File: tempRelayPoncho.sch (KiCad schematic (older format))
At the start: 2 parts

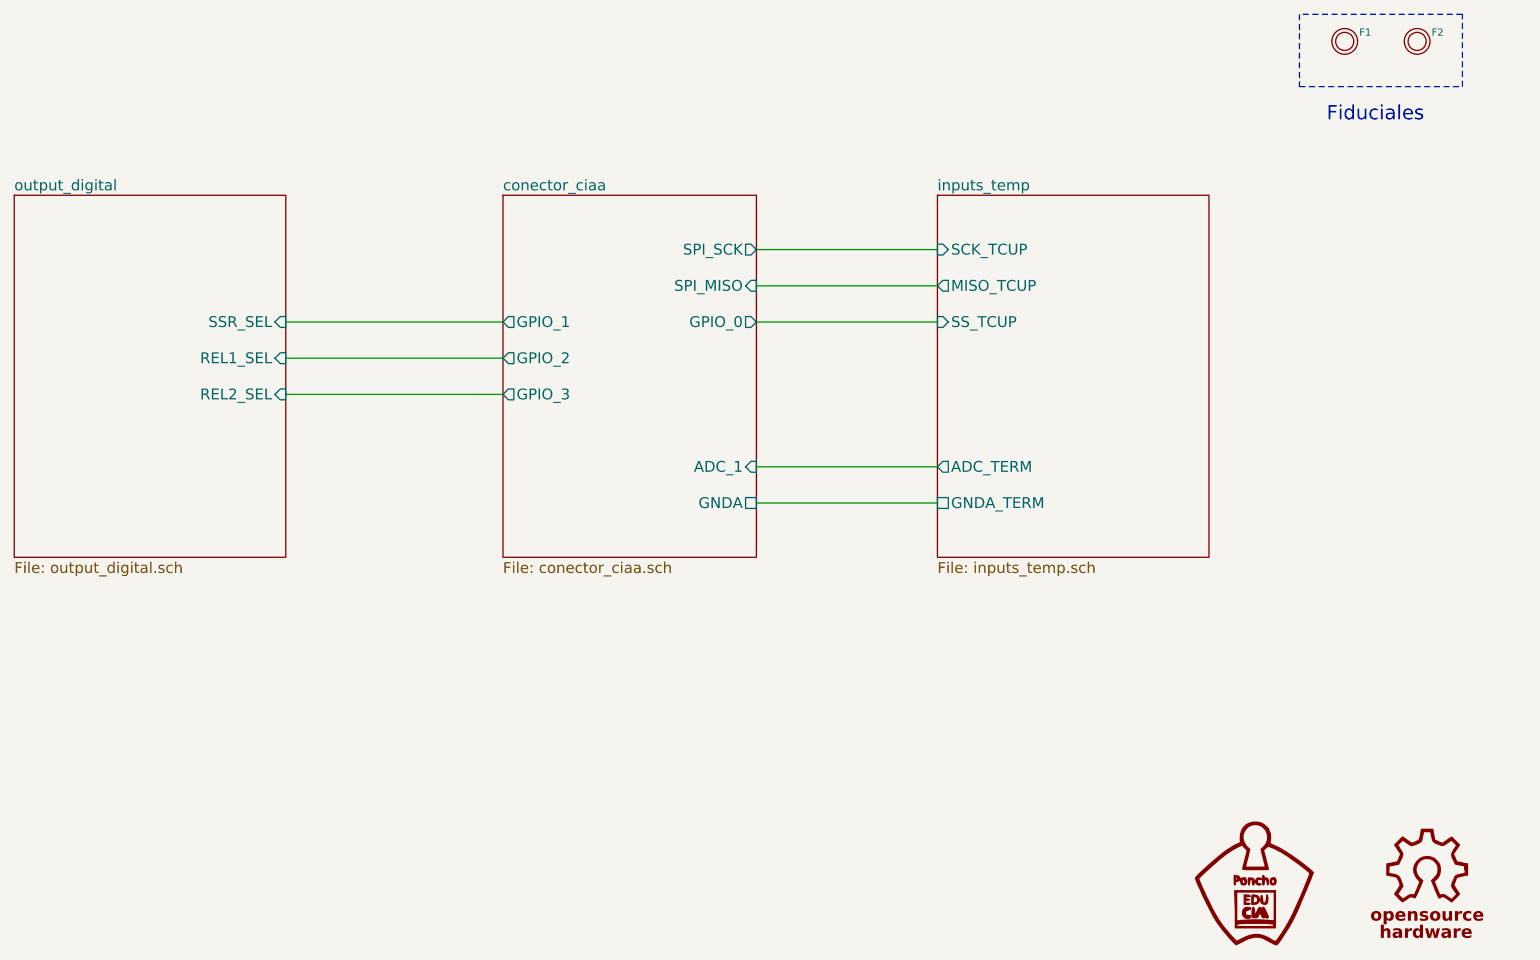
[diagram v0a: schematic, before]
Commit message: Primer version del PCB
Se agregan modificaciones segun primer correccion. Se carga primer version  del PCB.
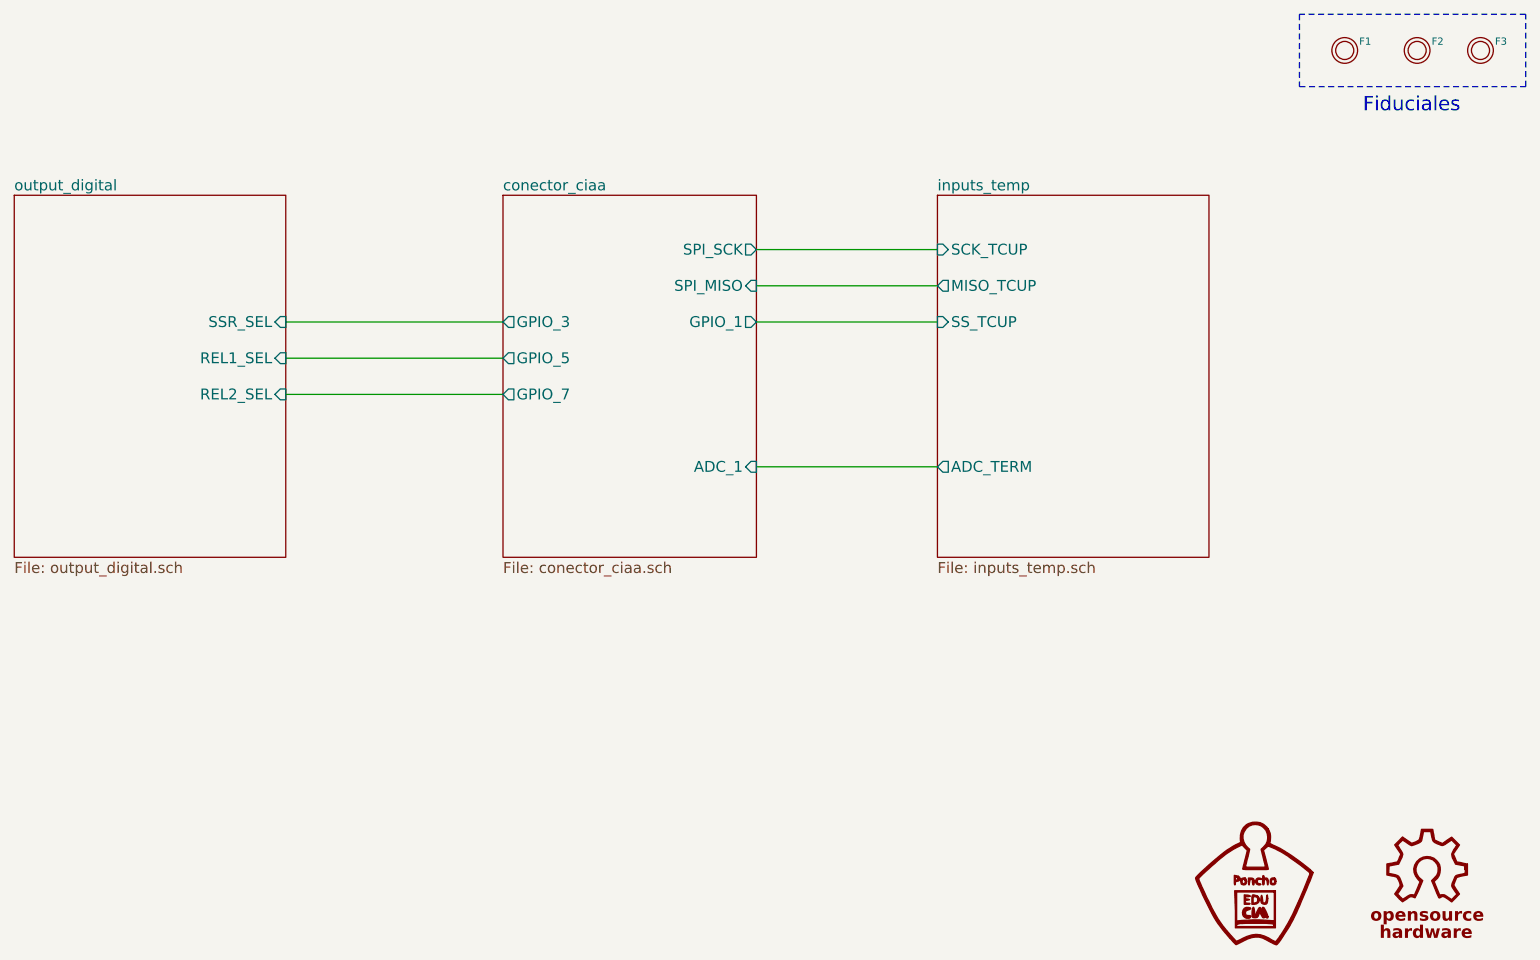
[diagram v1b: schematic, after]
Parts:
- added F3: FIDUCIAL, footprints:Fiducial_1mm, symbol FIDUCIAL
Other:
- moved on the sheet: F1, F2
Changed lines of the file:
@@
 EESchema Schematic File Version 2
 LIBS:TempRelay
+LIBS:power
 LIBS:tempRelayPoncho-cache
 EELAYER 25 0
@@
 Date "2017-06-14"
 Rev "1.0"
-Comp "Autor: Francisco Suárez"
-Comment1 "Revisor:  Mariano Orlante"
-Comment2 "Licencia: 'Docs/Licencia.txt\""
-Comment3 ""
+Comp "CESE - Trabajo final de la materia \"Diseño de Circuitos Impresos\""
+Comment1 "Licencia: 'Docs/Licencia.txt\""
+Comment2 "Revisor:  Mariano Orlante "
+Comment3 "Autor: Francisco Suárez"
 Comment4 ""
 $EndDescr
-$Sheet
-S 5200 2200 1400 2000
-U 59498167
-F0 "conector_ciaa" 60
-F1 "conector_ciaa.sch" 60
-F2 "GPIO_0" O R 6600 2900 60
-F3 "GPIO_2" O L 5200 3100 60
-F4 "GPIO_1" O L 5200 2900 60
-F5 "GPIO_3" O L 5200 3300 60
-F6 "SPI_MISO" I R 6600 2700 60
-F7 "ADC_1" I R 6600 3700 60
-F8 "SPI_SCK" O R 6600 2500 60
-F9 "GNDA" U R 6600 3900 60
-$EndSheet
-$Sheet
-S 7600 2200 1500 2000
-U 5949816A
-F0 "inputs_temp" 60
-F1 "inputs_temp.sch" 60
-F2 "ADC_TERM" O L 7600 3700 60
-F3 "MISO_TCUP" O L 7600 2700 60
-F4 "SS_TCUP" I L 7600 2900 60
-F5 "SCK_TCUP" I L 7600 2500 60
-F6 "GNDA_TERM" U L 7600 3900 60
-$EndSheet
 $Sheet
 S 2500 2200 1500 2000
@@
 L FIDUCIAL F1
 U 1 1 594EF035
-P 9850 1350
-F 0 "F1" H 9930 1400 40  0000 L CNN
-F 1 "FIDUCIAL" H 9850 1250 30  0001 C CNN
-F 2 "footprints:Fiducial_1mm" H 9850 1400 60  0001 C CNN
-F 3 "" H 9850 1400 60  0001 C CNN
-F 4 "FIDUCIAL" H 9900 1150 60  0001 C CNN "Descripcion"
-	1    9850 1350
+P 9850 1400
+F 0 "F1" H 9930 1450 40  0000 L CNN
+F 1 "FIDUCIAL" H 9850 1300 30  0001 C CNN
+F 2 "footprints:Fiducial_1mm" H 9850 1450 60  0001 C CNN
+F 3 "" H 9850 1450 60  0001 C CNN
+F 4 "FIDUCIAL" H 9900 1200 60  0001 C CNN "Descripcion"
+	1    9850 1400
 	1    0    0    -1
 $EndComp
@@
 L FIDUCIAL F2
 U 1 1 594EF17A
-P 10250 1350
-F 0 "F2" H 10330 1400 40  0000 L CNN
-F 1 "FIDUCIAL" H 10250 1250 30  0001 C CNN
-F 2 "footprints:Fiducial_1mm" H 10250 1400 60  0001 C CNN
-F 3 "" H 10250 1400 60  0001 C CNN
-F 4 "FIDUCIAL" H 10300 1150 60  0001 C CNN "Descripcion"
-	1    10250 1350
+P 10250 1400
+F 0 "F2" H 10330 1450 40  0000 L CNN
+F 1 "FIDUCIAL" H 10250 1300 30  0001 C CNN
+F 2 "footprints:Fiducial_1mm" H 10250 1450 60  0001 C CNN
+F 3 "" H 10250 1450 60  0001 C CNN
+F 4 "FIDUCIAL" H 10300 1200 60  0001 C CNN "Descripcion"
+	1    10250 1400
 	1    0    0    -1
 $EndComp
@@
 	9600 1200 9600 1600
 Wire Notes Line
-	9600 1600 10500 1600
+	9600 1600 10850 1600
 Wire Notes Line
-	10500 1600 10500 1200
+	10850 1600 10850 1200
 Wire Notes Line
-	10500 1200 9600 1200
-Text Notes 9750 1800 0    79   ~ 0
+	10850 1200 9600 1200
+Text Notes 9950 1750 0    79   ~ 0
 Fiduciales
-Wire Wire Line
-	6600 3900 7600 3900
 $Comp
 L Logo_Poncho #G1
@@
 F 0 "#G1" H 9300 5600 60  0001 C CNN
 F 1 "Logo_Poncho" H 9550 5600 60  0001 C CNN
-F 2 "" H 9350 6000 60  0000 C CNN
+F 2 "footprints:Logo_Poncho" H 9350 6000 60  0001 C CNN
 F 3 "" H 9350 6000 60  0000 C CNN
 F 4 "Value" H 9350 6000 60  0001 C CNN "Manf"
@@
 F 0 "#G2" H 10270 6400 60  0001 C CNN
 F 1 "OSHWA" H 10300 6303 60  0001 C CNN
-F 2 "" H 10300 6000 60  0000 C CNN
+F 2 "footprints:Logo_OSHWA" H 10300 6000 60  0001 C CNN
 F 3 "" H 10300 6000 60  0000 C CNN
+F 4 "Value" H 10300 6000 60  0001 C CNN "Manf"
+F 5 "Value" H 10300 6000 60  0001 C CNN "Manf#"
+F 6 "Value" H 10300 6000 60  0001 C CNN "Digikey#"
+F 7 "Value" H 10300 6000 60  0001 C CNN "Mouser#"
+F 8 "Value" H 10300 6000 60  0001 C CNN "Description"
 	1    10300 6000
 	1    0    0    -1
 $EndComp
+$Sheet
+S 5200 2200 1400 2000
+U 59498167
+F0 "conector_ciaa" 60
+F1 "conector_ciaa.sch" 60
+F2 "SPI_MISO" I R 6600 2700 60
+F3 "ADC_1" I R 6600 3700 60
+F4 "SPI_SCK" O R 6600 2500 60
+F5 "GPIO_1" O R 6600 2900 60
+F6 "GPIO_5" O L 5200 3100 60
+F7 "GPIO_3" O L 5200 2900 60
+F8 "GPIO_7" O L 5200 3300 60
+$EndSheet
+$Sheet
+S 7600 2200 1500 2000
+U 5949816A
+F0 "inputs_temp" 60
+F1 "inputs_temp.sch" 60
+F2 "ADC_TERM" O L 7600 3700 60
+F3 "MISO_TCUP" O L 7600 2700 60
+F4 "SS_TCUP" I L 7600 2900 60
+F5 "SCK_TCUP" I L 7600 2500 60
+$EndSheet
+$Comp
+L FIDUCIAL F3
+U 1 1 59641341
+P 10600 1400
+F 0 "F3" H 10680 1450 40  0000 L CNN
+F 1 "FIDUCIAL" H 10600 1300 30  0001 C CNN
+F 2 "footprints:Fiducial_1mm" H 10600 1450 60  0001 C CNN
+F 3 "" H 10600 1450 60  0001 C CNN
+F 4 "FIDUCIAL" H 10650 1200 60  0001 C CNN "Descripcion"
+	1    10600 1400
+	1    0    0    -1
+$EndComp

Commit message: Correccion Final
Se trabajo sobre correcciones de 2da revision. Se agregaron archivos gerbers, BOM, y objetos 3D
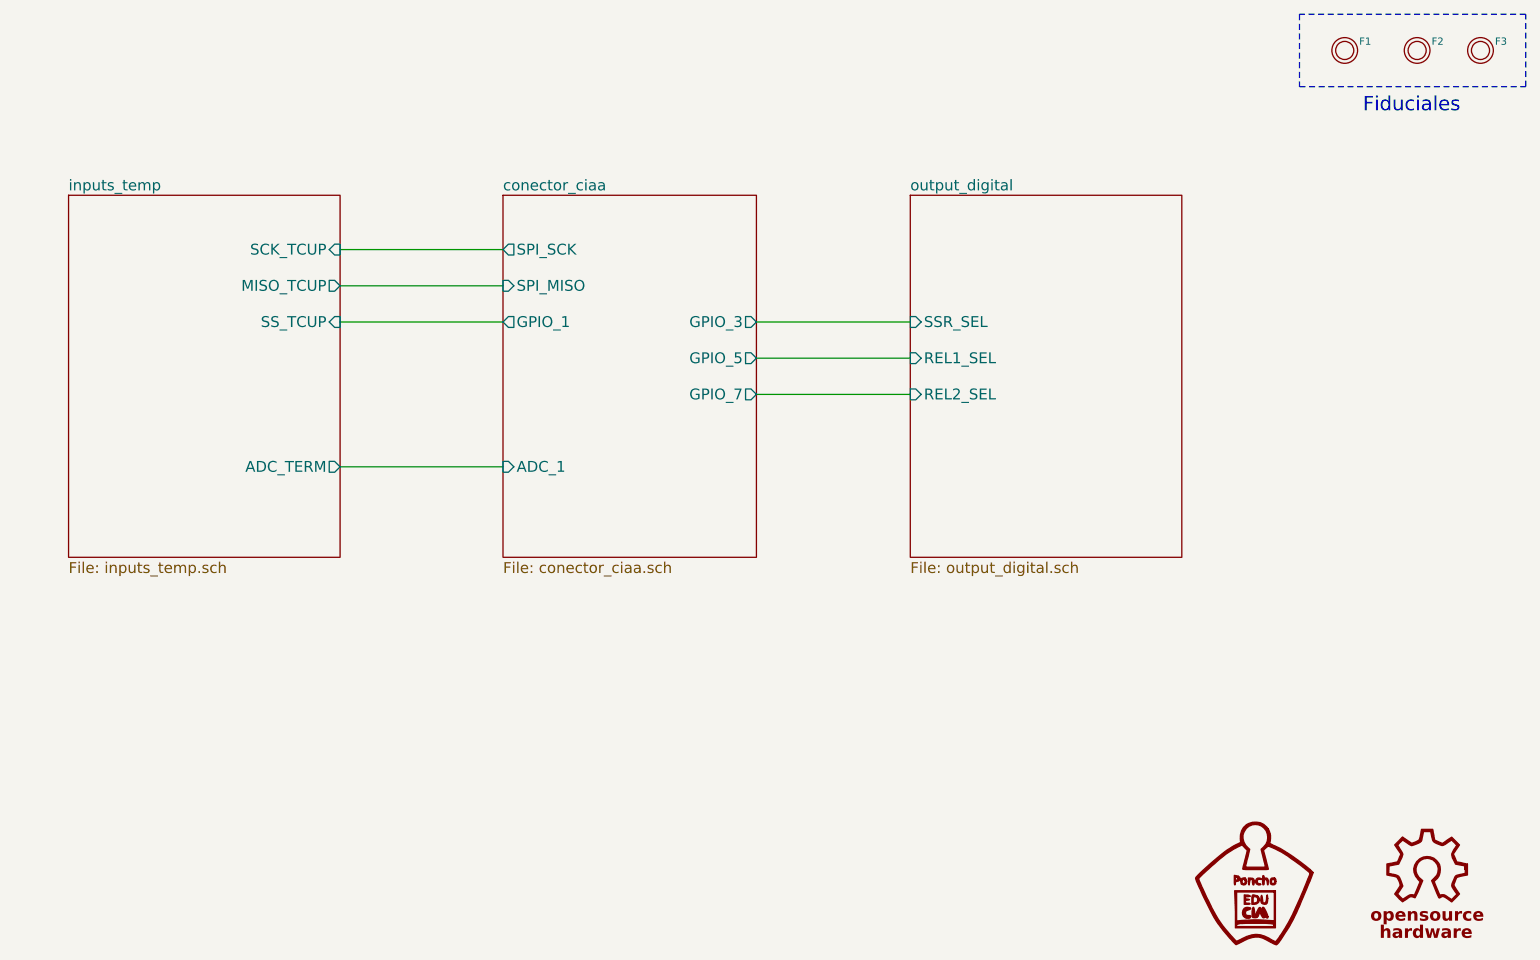
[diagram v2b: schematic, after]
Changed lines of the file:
@@
 EESchema Schematic File Version 2
 LIBS:TempRelay
-LIBS:power
-LIBS:tempRelayPoncho-cache
 EELAYER 25 0
 EELAYER END
@@
 $EndDescr
 $Sheet
-S 2500 2200 1500 2000
+S 7450 2200 1500 2000
 U 5949816D
 F0 "output_digital" 60
 F1 "output_digital.sch" 60
-F2 "SSR_SEL" I R 4000 2900 60
-F3 "REL1_SEL" I R 4000 3100 60
-F4 "REL2_SEL" I R 4000 3300 60
+F2 "SSR_SEL" I L 7450 2900 60
+F3 "REL1_SEL" I L 7450 3100 60
+F4 "REL2_SEL" I L 7450 3300 60
 $EndSheet
-Wire Wire Line
-	6600 2500 7600 2500
-Wire Wire Line
-	7600 2700 6600 2700
-Wire Wire Line
-	6600 2900 7600 2900
-Wire Wire Line
-	7600 3700 6600 3700
-Wire Wire Line
-	5200 2900 4000 2900
-Wire Wire Line
-	5200 3100 4000 3100
-Wire Wire Line
-	5200 3300 4000 3300
 $Comp
 L FIDUCIAL F1
@@
 F0 "conector_ciaa" 60
 F1 "conector_ciaa.sch" 60
-F2 "SPI_MISO" I R 6600 2700 60
-F3 "ADC_1" I R 6600 3700 60
-F4 "SPI_SCK" O R 6600 2500 60
-F5 "GPIO_1" O R 6600 2900 60
-F6 "GPIO_5" O L 5200 3100 60
-F7 "GPIO_3" O L 5200 2900 60
-F8 "GPIO_7" O L 5200 3300 60
+F2 "SPI_MISO" I L 5200 2700 60
+F3 "ADC_1" I L 5200 3700 60
+F4 "SPI_SCK" O L 5200 2500 60
+F5 "GPIO_1" O L 5200 2900 60
+F6 "GPIO_5" O R 6600 3100 60
+F7 "GPIO_3" O R 6600 2900 60
+F8 "GPIO_7" O R 6600 3300 60
 $EndSheet
 $Sheet
-S 7600 2200 1500 2000
+S 2800 2200 1500 2000
 U 5949816A
 F0 "inputs_temp" 60
 F1 "inputs_temp.sch" 60
-F2 "ADC_TERM" O L 7600 3700 60
-F3 "MISO_TCUP" O L 7600 2700 60
-F4 "SS_TCUP" I L 7600 2900 60
-F5 "SCK_TCUP" I L 7600 2500 60
+F2 "ADC_TERM" O R 4300 3700 60
+F3 "MISO_TCUP" O R 4300 2700 60
+F4 "SS_TCUP" I R 4300 2900 60
+F5 "SCK_TCUP" I R 4300 2500 60
 $EndSheet
 $Comp
@@
 	1    0    0    -1
 $EndComp
+Wire Wire Line
+	5200 2500 4300 2500
+Wire Wire Line
+	4300 2700 5200 2700
+Wire Wire Line
+	5200 2900 4300 2900
+Wire Wire Line
+	4300 3700 5200 3700
+Wire Wire Line
+	6600 2900 7450 2900
+Wire Wire Line
+	6600 3100 7450 3100
+Wire Wire Line
+	6600 3300 7450 3300
 $EndSCHEMATC
